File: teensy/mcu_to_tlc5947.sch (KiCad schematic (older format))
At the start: 32 parts, among them J1 conn_1x2, J10 conn_1x2, J11 conn_1x2, J12 conn_1x2, J13 conn_1x2, J14 conn_1x2, J15 conn_1x2, J16 conn_1x2, J17 conn_1x2, J18 conn_1x2, J19 conn_1x2, J2 conn_2x2_odd_even, J20 conn_1x2, J21 conn_1x2, J22 conn_1x2, J23 conn_1x2, J24 conn_1x2, J25 conn_1x2, J26 conn_1x2, J27 conn_1x2, J28 conn_1x2, J29 conn_1x2, J3 conn_2x13_odd_even, J30 conn_1x2, J4 conn_2x3_odd_even, J5 conn_2x5_odd_even, J6 conn_2x5_odd_even, J7 conn_1x2, J8 conn_1x2, J9 conn_1x2, U1 TEENSY3.1, U2 Adafruit_TLC5947

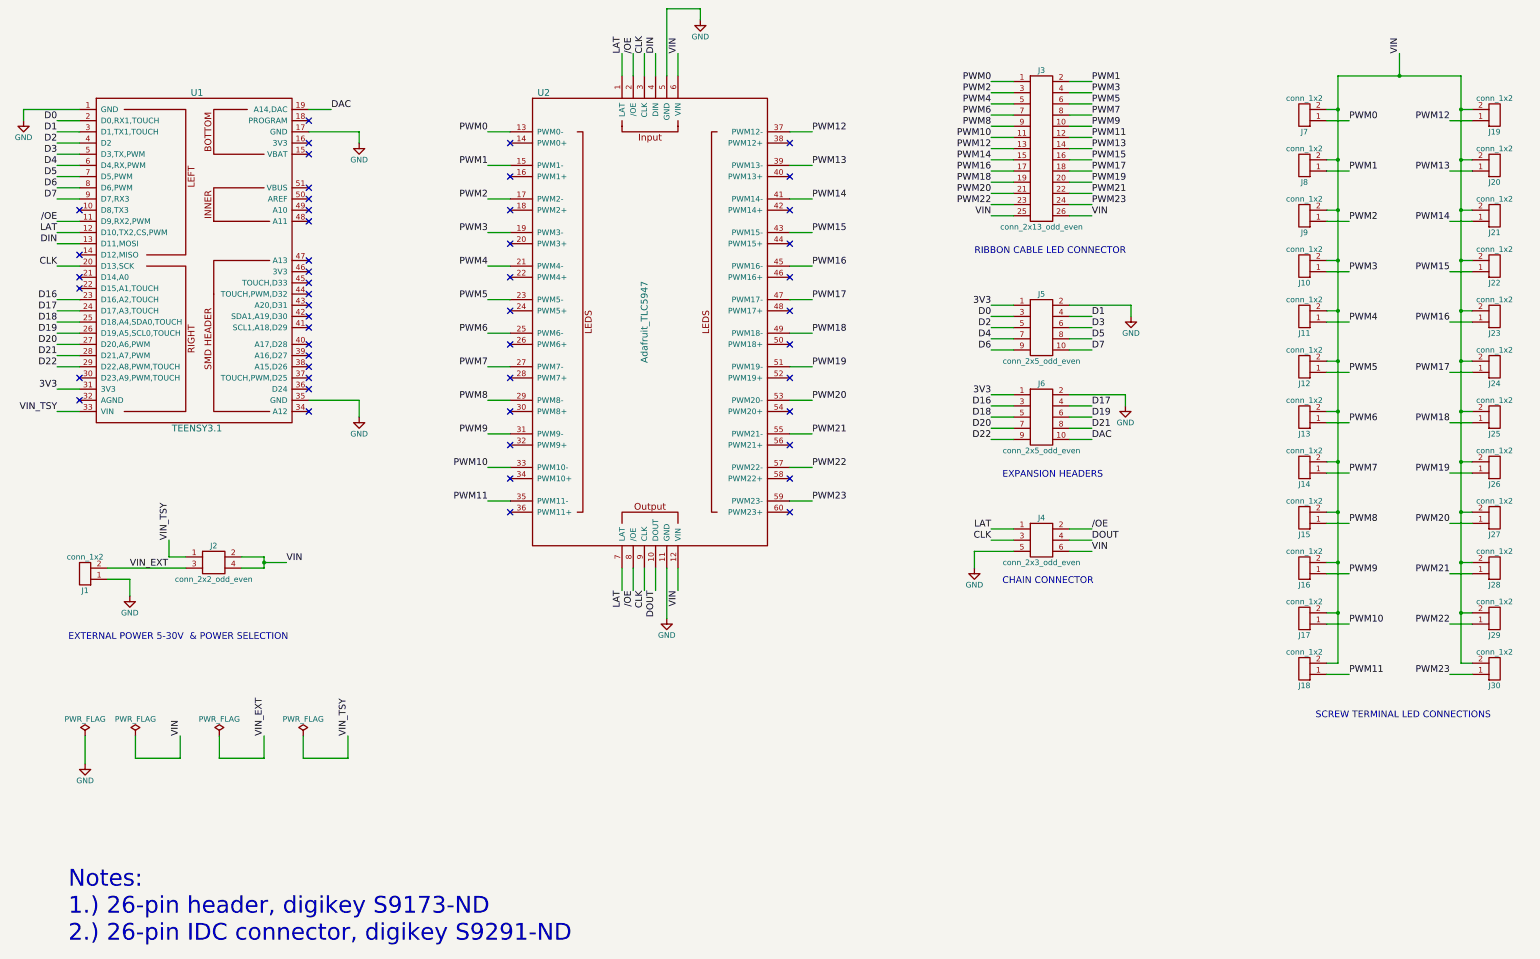
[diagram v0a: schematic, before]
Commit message: Completed initial version of design. Created version 0.1 gerber files.
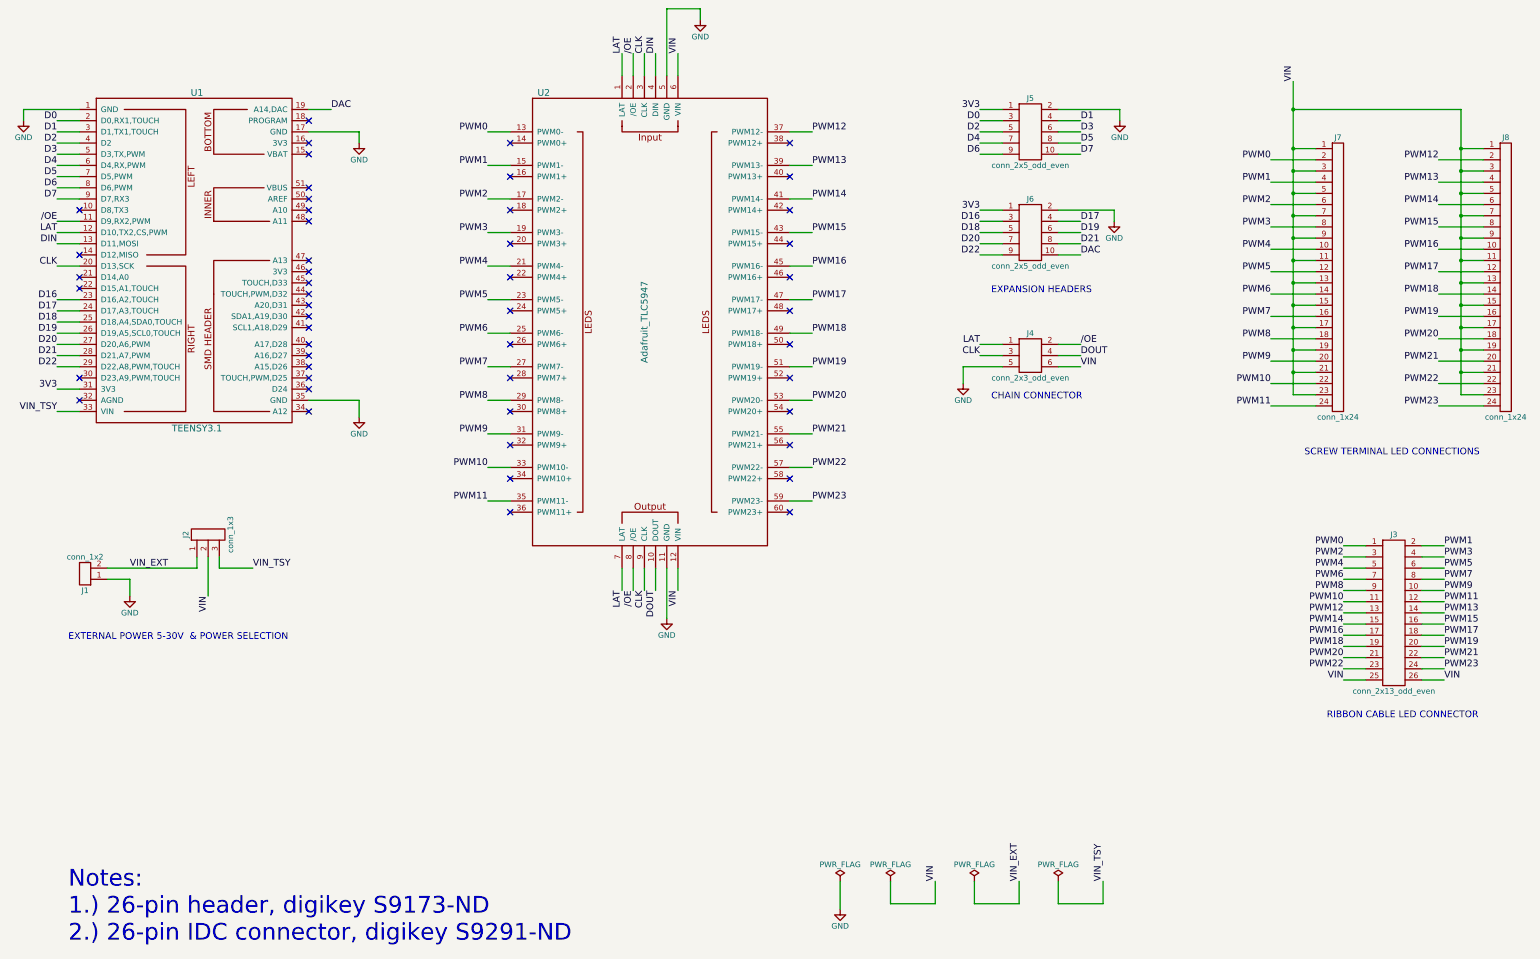
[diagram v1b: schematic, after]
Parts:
- removed J10, J11, J12, J13, J14, J15, J16, J17, J18, J19, J20, J21, J22, J23, J24, J25, J26, J27, J28, J29, J30, J7, J8, J9: conn_1x2, symbol conn_1x2
- removed J2: conn_2x2_odd_even, symbol conn_2x2_odd_even
- added J2: conn_1x3, PIN_ARRAY_1X3:PIN_ARRAY_1X3, symbol conn_1x3
- added J7, J8: conn_1x24, BLOCK_CONN_24:BLOCK_CONN_2X1, symbol conn_1x24
- J1: footprint (none) -> BLOCK_CONN_2:BLOCK_CONN_2X1
- J3: footprint (none) -> 13X2_SHRD_HEADER:5X2_SHRD_HEADER
- J4: footprint (none) -> 3X2_SHRD_HEADER:3X2_SHRD_HEADER
- J5, J6: footprint (none) -> 5X2_SHRD_HEADER:5X2_SHRD_HEADER
- U1: footprint (none) -> Teensy3x:TEENSY3X
- U2: footprint (none) -> Adafruit_TLC5947:Adafruit_TLC5947
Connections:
- net PWM0: now also J7.2 (Pin_2)
- net PWM1: now also J7.4 (Pin_4)
- net PWM10: now also J7.22 (Pin_22)
- net PWM11: now also J7.24 (Pin_24)
- net PWM12: now also J8.2 (Pin_2)
- net PWM13: now also J8.4 (Pin_4)
- net PWM14: now also J8.6 (Pin_6)
- net PWM15: now also J8.8 (Pin_8)
- net PWM16: now also J8.10 (Pin_10)
- net PWM17: now also J8.12 (Pin_12)
- net PWM18: now also J8.14 (Pin_14)
- net PWM19: now also J8.16 (Pin_16)
- net PWM2: now also J7.6 (Pin_6)
- net PWM20: now also J8.18 (Pin_18)
- net PWM21: now also J8.20 (Pin_20)
- net PWM22: now also J8.22 (Pin_22)
- net PWM23: now also J8.24 (Pin_24)
- net PWM3: now also J7.8 (Pin_8)
- net PWM4: now also J7.10 (Pin_10)
- net PWM5: now also J7.12 (Pin_12)
- net PWM6: now also J7.14 (Pin_14)
- net PWM7: now also J7.16 (Pin_16)
- net PWM8: now also J7.18 (Pin_18)
- net PWM9: now also J7.20 (Pin_20)
- net VIN: now also J2.2 (Pin_2), J7.1 (Pin_1), J7.11 (Pin_11), J7.13 (Pin_13), J7.15 (Pin_15), J7.17 (Pin_17), J7.19 (Pin_19), J7.21 (Pin_21), J7.23 (Pin_23), J7.3 (Pin_3), J7.5 (Pin_5), J7.7 (Pin_7), J7.9 (Pin_9), J8.1 (Pin_1), J8.11 (Pin_11), J8.13 (Pin_13), J8.15 (Pin_15), J8.17 (Pin_17), J8.19 (Pin_19), J8.21 (Pin_21), J8.23 (Pin_23), J8.3 (Pin_3), J8.5 (Pin_5), J8.7 (Pin_7), J8.9 (Pin_9)
- net VIN_EXT: now also J2.1 (Pin_1)
- net VIN_TSY: now also J2.3 (Pin_3)
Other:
- moved on the sheet: J3, J4, J5, J6
